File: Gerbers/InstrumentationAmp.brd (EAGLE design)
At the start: 22.5 x 49.6 mm, 49 parts, among them IC1 AD623R, Q1 310mA/60V/1.6Ω, Q2 310mA/60V/1.6Ω

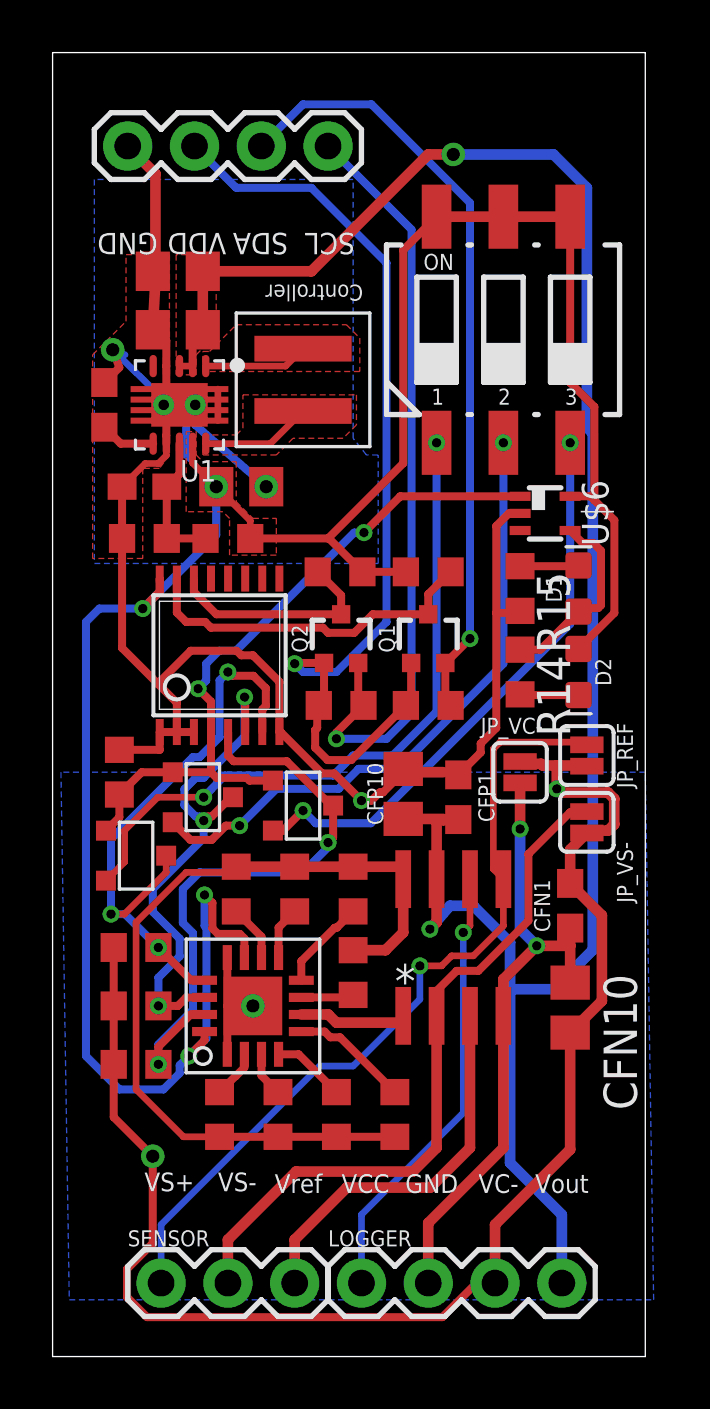
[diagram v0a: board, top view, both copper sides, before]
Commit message: changes to header and silkscreen labels
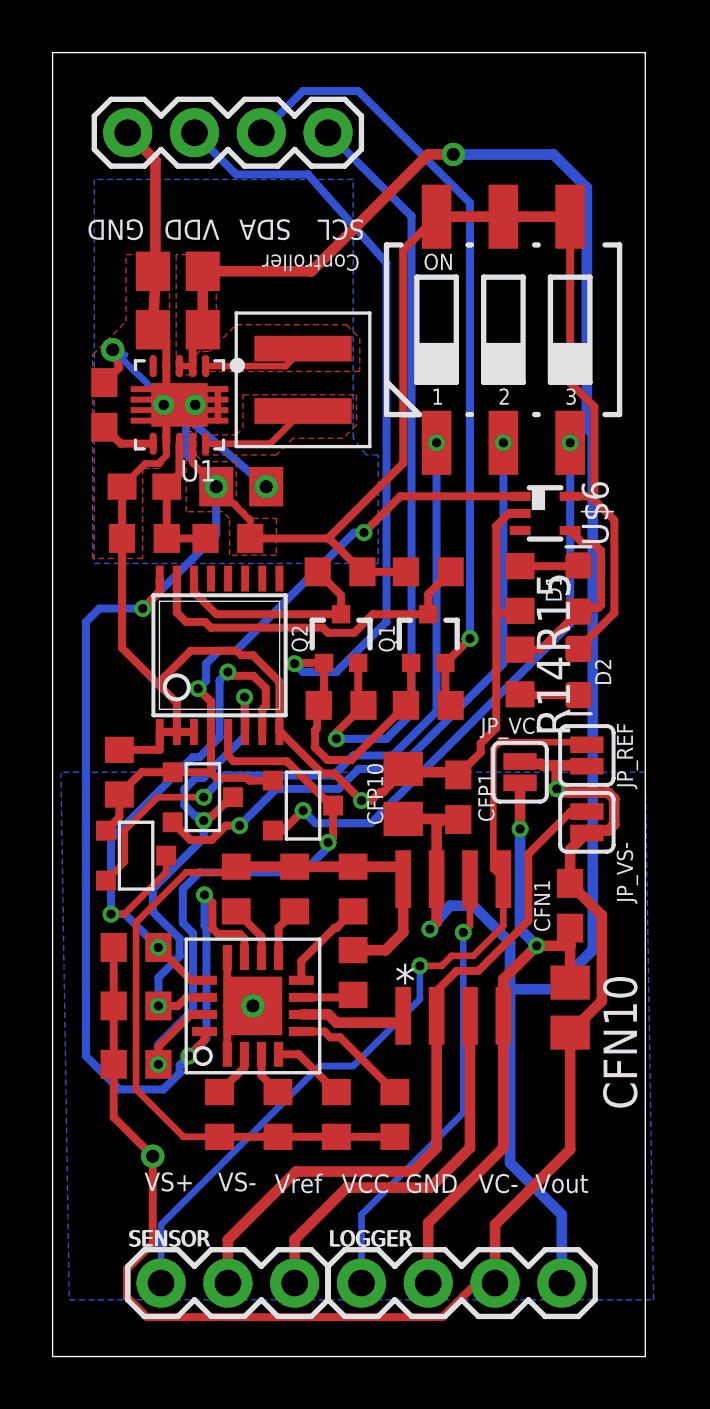
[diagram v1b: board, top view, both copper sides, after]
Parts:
- moved J1 0.51 mm to (1.59, 45.3)
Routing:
- net GND: track 132.8 -> 133.3 mm
- net SCL_OUT: track 29.7 -> 30.2 mm
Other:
- board text added: "LOGGER"
- board text added: "SENSOR"
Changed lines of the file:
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@@
 <?xml version="1.0" encoding="utf-8"?>
 <!DOCTYPE eagle SYSTEM "eagle.dtd">
-<eagle version="8.3.0">
+<eagle version="8.4.0">
 <drawing>
 <settings>
@@
 <setting verticaltext="up"/>
 </settings>
-<grid distance="50" unitdist="mil" unit="mm" style="lines" multiple="1" display="yes" altdistance="5" altunitdist="mil" altunit="mm"/>
+<grid distance="0.127" unitdist="mm" unit="mm" style="lines" multiple="1" display="yes" altdistance="5" altunitdist="mil" altunit="mm"/>
 <layers>
 <layer number="1" name="Top" color="4" fill="1" visible="yes" active="yes"/>
@@
 <layer number="110" name="fp0" color="7" fill="1" visible="no" active="yes"/>
 <layer number="111" name="LPC17xx" color="7" fill="1" visible="no" active="yes"/>
-<layer number="112" name="tSilk" color="7" fill="1" visible="no" active="yes"/>
+<layer number="112" name="tSilk" color="7" fill="1" visible="yes" active="yes"/>
 <layer number="113" name="IDFDebug" color="4" fill="1" visible="no" active="yes"/>
 <layer number="114" name="Badge_Outline" color="7" fill="1" visible="no" active="yes"/>
@@
 <text x="7.1755" y="4.953" size="0.7112" layer="112">Vref</text>
 <text x="11.7475" y="12.3825" size="1.27" layer="21">*</text>
-<text x="10.2235" y="41.4655" size="0.8128" layer="112" rot="SR180">SCL</text>
-<text x="7.6835" y="41.4655" size="0.8128" layer="112" rot="SR180">SDA</text>
-<text x="5.334" y="41.4655" size="0.8128" layer="112" rot="SR180">VDD</text>
-<text x="2.7305" y="41.4655" size="0.8128" layer="112" rot="SR180">GND</text>
-<text x="10.541" y="39.497" size="0.6096" layer="112" font="vector" ratio="20" rot="SR180">Controller</text>
+<text x="10.6045" y="41.9735" size="0.7712" layer="112" rot="SR180">SCL</text>
+<text x="7.8105" y="41.9735" size="0.7712" layer="112" rot="SR180">SDA</text>
+<text x="5.08" y="41.9735" size="0.7712" layer="112" rot="SR180">VDD</text>
+<text x="2.2225" y="41.9735" size="0.7712" layer="112" rot="SR180">GND</text>
+<text x="10.414" y="40.64" size="0.6096" layer="112" font="vector" ratio="20" rot="SR180">Controller</text>
 <rectangle x1="1.27" y1="-1.397" x2="19.685" y2="4.699" layer="39"/>
-<rectangle x1="-0.889" y1="41.529" x2="11.811" y2="48.006" layer="39"/>
+<rectangle x1="-0.889" y1="42.037" x2="11.811" y2="48.514" layer="39"/>
 <text x="20.32" y="36.83" size="1.27" layer="122" font="vector" rot="MR0">InstAmp
 Bobby Schulz
 v1.1
 11/06/2017</text>
+<text x="9.271" y="2.921" size="0.6096" layer="112" font="vector" ratio="20" rot="SR0">LOGGER</text>
+<text x="1.651" y="2.921" size="0.6096" layer="112" font="vector" ratio="20" rot="SR0">SENSOR</text>
 </plain>
 <attributes>
@@
 <param name="dpMaxLengthDifference" value="10mm"/>
 <param name="dpGapFactor" value="2.5"/>
-<param name="checkGrid" value="0"/>
-<param name="checkAngle" value="0"/>
 <param name="checkFont" value="1"/>
 <param name="checkRestrict" value="1"/>
+<param name="checkStop" value="0"/>
 <param name="useDiameter" value="13"/>
 <param name="maxErrors" value="50"/>
@@
 <attribute name="VALUE" x="14.605" y="28.575" size="1.27" layer="27" rot="R270"/>
 </element>
-<element name="J1" library="SparkFun-Connectors" package="1X04" value="" x="1.5875" y="44.7675" smashed="yes">
-<attribute name="VALUE" x="0.3175" y="42.7355" size="0.6096" layer="27" font="vector" ratio="20"/>
+<element name="J1" library="SparkFun-Connectors" package="1X04" value="" x="1.5875" y="45.2755" smashed="yes">
+<attribute name="VALUE" x="0.3175" y="43.2435" size="0.6096" layer="27" font="vector" ratio="20"/>
 </element>
 <element name="Q1" library="SparkFun-DiscreteSemi" package="SOT323" value="310mA/60V/1.6Ω" x="13.0175" y="26.035" smashed="yes">
@@
 <vertex x="1.524" y="40.64"/>
 </polygon>
-<wire x1="1.5875" y1="44.7675" x2="2.6425" y2="43.7125" width="0.4064" layer="1"/>
-<wire x1="2.6425" y1="43.7125" x2="2.6425" y2="39.709571875" width="0.4064" layer="1"/>
+<wire x1="1.5875" y1="45.2755" x2="2.6425" y2="44.2205" width="0.4064" layer="1"/>
+<wire x1="2.6425" y1="44.2205" x2="2.6425" y2="39.709571875" width="0.4064" layer="1"/>
 <wire x1="10.4775" y1="19.8755" x2="10.85810625" y2="19.8755" width="0.3048" layer="1"/>
 <wire x1="11.16770625" y1="20.1851" x2="11.2951" y2="20.1851" width="0.3048" layer="1"/>
@@
 <wire x1="11.43" y1="26.67" x2="9.525" y2="24.765" width="0.3048" layer="16"/>
 <wire x1="11.43" y1="26.67" x2="11.43" y2="40.3225" width="0.3048" layer="16"/>
-<wire x1="11.43" y1="40.3225" x2="8.5725" y2="43.18" width="0.3048" layer="16"/>
-<wire x1="8.5725" y1="43.18" x2="5.715" y2="43.18" width="0.3048" layer="16"/>
-<wire x1="5.715" y1="43.18" x2="4.1275" y2="44.7675" width="0.3048" layer="16"/>
+<wire x1="11.43" y1="40.3225" x2="8.4455" y2="43.688" width="0.3048" layer="16"/>
+<wire x1="8.4455" y1="43.688" x2="5.715" y2="43.688" width="0.3048" layer="16"/>
+<wire x1="5.715" y1="43.688" x2="4.1275" y2="45.2755" width="0.3048" layer="16"/>
 <wire x1="8.794340625" y1="23.434840625" x2="8.8545" y2="23.495" width="0.3048" layer="1" curve="-90"/>
 <wire x1="8.7162" y1="21.88998125" x2="9.18998125" y2="21.4162" width="0.3048" layer="1"/>
@@
 <wire x1="9.525" y1="22.225" x2="11.43" y2="22.225" width="0.3048" layer="16"/>
 <wire x1="11.43" y1="22.225" x2="12.3825" y2="23.1775" width="0.3048" layer="16"/>
-<wire x1="12.3825" y1="41.5925" x2="9.2075" y2="44.7675" width="0.3048" layer="16"/>
-<wire x1="12.3825" y1="23.1775" x2="12.3825" y2="41.5925" width="0.3048" layer="16"/>
+<wire x1="12.3825" y1="42.1005" x2="9.2075" y2="45.2755" width="0.3048" layer="16"/>
+<wire x1="12.3825" y1="23.1775" x2="12.3825" y2="42.1005" width="0.3048" layer="16"/>
 </signal>
 <signal name="SDA_OUT">
@@
 <via x="14.605" y="26.035" extent="1-16" drill="0.35" shape="octagon"/>
 <wire x1="14.605" y1="26.035" x2="14.605" y2="42.6085" width="0.3048" layer="16"/>
-<wire x1="14.605" y1="42.6085" x2="10.8585" y2="46.355" width="0.3048" layer="16"/>
-<wire x1="10.8585" y1="46.355" x2="8.255" y2="46.355" width="0.3048" layer="16"/>
-<wire x1="8.255" y1="46.355" x2="6.6675" y2="44.7675" width="0.3048" layer="16"/>
+<wire x1="14.605" y1="42.6085" x2="10.3505" y2="46.863" width="0.3048" layer="16"/>
+<wire x1="10.3505" y1="46.863" x2="8.255" y2="46.863" width="0.3048" layer="16"/>
+<wire x1="8.255" y1="46.863" x2="6.6675" y2="45.2755" width="0.3048" layer="16"/>
 </signal>
 <signal name="N$19">
